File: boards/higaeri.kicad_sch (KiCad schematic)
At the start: 0 parts

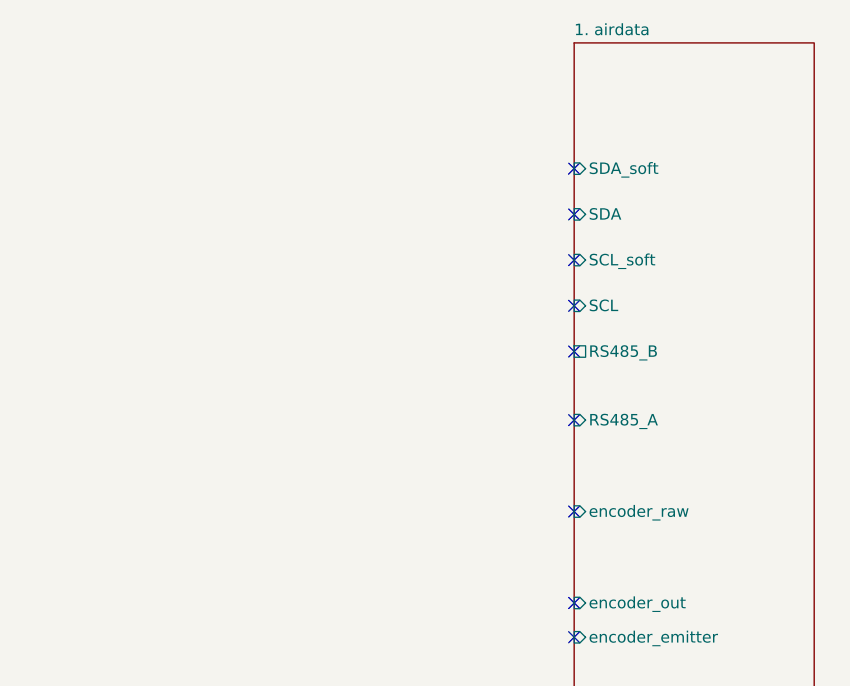
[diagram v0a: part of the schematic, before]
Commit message: 増幅回路追加
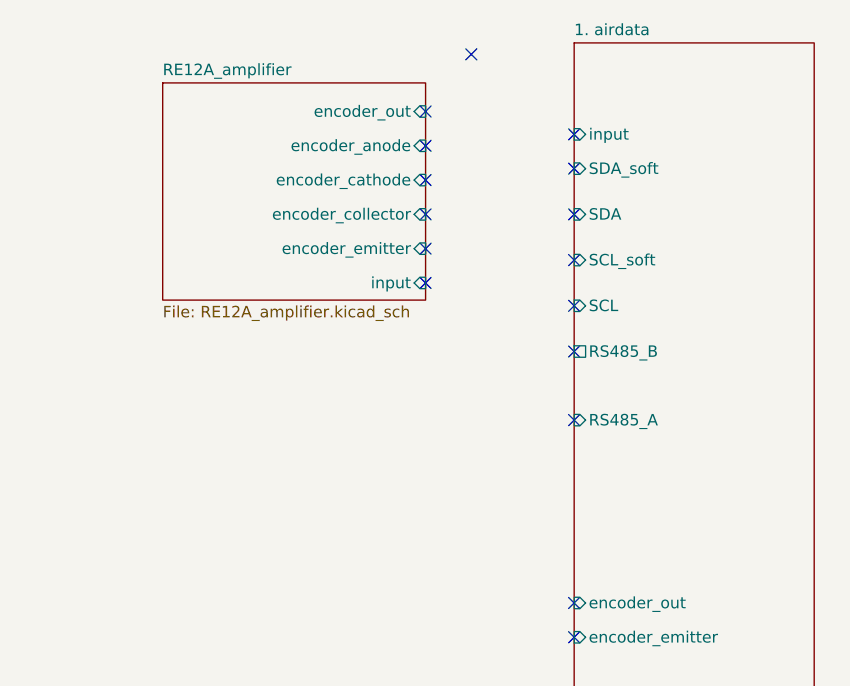
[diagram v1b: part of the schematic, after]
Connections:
- no-connect marks 43 -> 50
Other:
- added sheet RE12A_amplifier (RE12A_amplifier.kicad_sch)
- sheet 1. airdata ports: added input; removed encoder_raw
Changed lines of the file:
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@@
+	)
+	(no_connect
+		(at 215.9 55.88)
 	)
 	(no_connect
@@
 	)
 	(no_connect
+		(at 220.98 30.48)
+	)
+	(no_connect
 		(at 99.06 66.04)
 	)
 	(no_connect
-		(at 232.41 81.28)
-	)
-	(no_connect
 		(at 232.41 63.5)
 	)
@@
 	)
 	(no_connect
+		(at 215.9 48.26)
+	)
+	(no_connect
+		(at 215.9 44.45)
+	)
+	(no_connect
 		(at 57.15 38.1)
 	)
 	(no_connect
+		(at 215.9 36.83)
+	)
+	(no_connect
+		(at 215.9 52.07)
+	)
+	(no_connect
 		(at 232.41 118.11)
 	)
@@
 	)
 	(no_connect
+		(at 232.41 39.37)
+	)
+	(no_connect
 		(at 232.41 132.08)
 	)
@@
 	(no_connect
 		(at 232.41 48.26)
+	)
+	(no_connect
+		(at 215.9 40.64)
 	)
 	(no_connect
@@
 		)
 		(instances
-			(project "26proto"
+			(project "higaeri"
 				(path "/493bec57-bd9f-4f18-b3ef-0d7a091ad475"
 					(page "3")
@@
 		)
 		(instances
-			(project "26proto"
+			(project "higaeri"
 				(path "/493bec57-bd9f-4f18-b3ef-0d7a091ad475"
 					(page "4")
+				)
+			)
+		)
+	)
+	(sheet
+		(at 186.69 33.655)
+		(size 29.21 24.13)
+		(exclude_from_sim no)
+		(in_bom yes)
+		(on_board yes)
+		(dnp no)
+		(fields_autoplaced yes)
+		(stroke
+			(width 0.1524)
+			(type solid)
+		)
+		(fill
+			(color 0 0 0 0.0000)
+		)
+		(property "Sheetname" "RE12A_amplifier"
+			(at 186.69 32.9434 0)
+			(effects
+				(font
+					(size 1.27 1.27)
+				)
+				(justify left bottom)
+			)
+		)
+		(property "Sheetfile" "RE12A_amplifier.kicad_sch"
+			(at 186.69 58.3696 0)
+			(effects
+				(font
+					(size 1.27 1.27)
+				)
+				(justify left top)
+			)
+		)
+		(pin "encoder_anode" input
+			(at 215.9 40.64 0)
+			(effects
+				(font
+					(size 1.27 1.27)
+				)
+				(justify right)
+			)
+		)
+		(pin "encoder_cathode" input
+			(at 215.9 44.45 0)
+			(effects
+				(font
+					(size 1.27 1.27)
+				)
+				(justify right)
+			)
+		)
+		(pin "encoder_collector" input
+			(at 215.9 48.26 0)
+			(effects
+				(font
+					(size 1.27 1.27)
+				)
+				(justify right)
+			)
+		)
+		(pin "encoder_emitter" input
+			(at 215.9 52.07 0)
+			(effects
+				(font
+					(size 1.27 1.27)
+				)
+				(justify right)
+			)
+		)
+		(pin "encoder_out" input
+			(at 215.9 36.83 0)
+			(effects
+				(font
+					(size 1.27 1.27)
+				)
+				(justify right)
+			)
+		)
+		(pin "input" input
+			(at 215.9 55.88 0)
+			(effects
+				(font
+					(size 1.27 1.27)
+				)
+				(justify right)
+			)
+		)
+		(instances
+			(project "higaeri"
+				(path "/493bec57-bd9f-4f18-b3ef-0d7a091ad475"
+					(page "5")
 				)
 			)
@@
 			)
 		)
-		(pin "encoder_raw" input
-			(at 232.41 81.28 180)
-			(effects
-				(font
-					(size 1.27 1.27)
-				)
-				(justify left)
-			)
-		)
 		(pin "RS485_A" input
 			(at 232.41 71.12 180)
@@
 			)
 		)
+		(pin "input" input
+			(at 232.41 39.37 180)
+			(effects
+				(font
+					(size 1.27 1.27)
+				)
+				(justify left)
+			)
+		)
 		(instances
-			(project "26proto"
+			(project "higaeri"
 				(path "/493bec57-bd9f-4f18-b3ef-0d7a091ad475"
 					(page "2")
